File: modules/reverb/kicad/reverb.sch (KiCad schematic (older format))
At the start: 67 parts, among them P1 CONN_01X02, P2 CONN_01X03, P3 CONN_01X02, P4 CONN_01X03, P5 CONN_01X03, P6 CONN_01X02, P7 CONN_01X02, P8 CONN_01X02, P9 CONN_01X02, Q1 2N3906, Q2 2N3906, U1 TL074, U2 TL074, U3 LM386, U4 LM13700

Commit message: Reverb PCB: footprint assignments
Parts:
- added C2, C3: 470u, Capacitors_ThroughHole:CP_Radial_D8.0mm_P3.50mm, symbol CP
- C1: footprint (none) -> Capacitors_ThroughHole:C_Disc_D4.7mm_W2.5mm_P5.00mm
- C10: renamed from C8; footprint (none) -> Capacitors_ThroughHole:C_Disc_D4.7mm_W2.5mm_P5.00mm
- C11: renamed from C9; footprint (none) -> Capacitors_ThroughHole:C_Disc_D4.7mm_W2.5mm_P5.00mm
- C12: renamed from C10; footprint (none) -> Capacitors_ThroughHole:CP_Radial_D4.0mm_P1.50mm
- C13: renamed from C11; footprint (none) -> Capacitors_ThroughHole:C_Disc_D4.7mm_W2.5mm_P5.00mm
- C14: renamed from C12; footprint (none) -> Capacitors_ThroughHole:CP_Radial_D10.0mm_P3.80mm
- C15: renamed from C13; footprint (none) -> Capacitors_ThroughHole:C_Disc_D4.7mm_W2.5mm_P5.00mm
- C16: renamed from C14; footprint (none) -> Capacitors_ThroughHole:C_Disc_D4.7mm_W2.5mm_P5.00mm
- C17: renamed from C15; footprint (none) -> Capacitors_ThroughHole:C_Disc_D4.7mm_W2.5mm_P5.00mm
- C18: renamed from C16; footprint (none) -> Capacitors_ThroughHole:C_Disc_D4.7mm_W2.5mm_P5.00mm
- C4: renamed from C2; footprint (none) -> Capacitors_ThroughHole:CP_Radial_D4.0mm_P1.50mm
- C5: renamed from C3; footprint (none) -> Capacitors_ThroughHole:CP_Radial_D4.0mm_P1.50mm
- C6: renamed from C4; footprint (none) -> Capacitors_ThroughHole:CP_Radial_D4.0mm_P1.50mm
- C7: renamed from C5; footprint (none) -> Capacitors_ThroughHole:CP_Radial_D4.0mm_P1.50mm
- C8: renamed from C6; footprint (none) -> Capacitors_ThroughHole:CP_Radial_D4.0mm_P1.50mm
- C9: renamed from C7; footprint (none) -> Capacitors_ThroughHole:CP_Radial_D4.0mm_P1.50mm
- D1, D2: footprint (none) -> Diodes_ThroughHole:D_DO-35_SOD27_P7.62mm_Horizontal
- P1, P3, P6, P7, P8, P9: footprint (none) -> Connectors_Molex:Molex_KK-6410-02_02x2.54mm_Straight
- P2, P4, P5: footprint (none) -> Connectors_Molex:Molex_KK-6410-03_03x2.54mm_Straight
- Q1, Q2: footprint (none) -> TO_SOT_Packages_THT:TO-92_Inline_Narrow_Oval
- R1, R10, R11, R12, R13, R14, R15, R16, R17, R18, R19, R2, R20, R21, R22, R23, R24, R25, R26, R27, R28, R29, R3, R30, R31, R32, R33, R34, R4, R5, R6, R7, R8, R9: footprint (none) -> Resistors_ThroughHole:R_Axial_DIN0207_L6.3mm_D2.5mm_P7.62mm_Horizontal
- U1: renamed from U2; footprint (none) -> Housings_DIP:DIP-14_W7.62mm_LongPads
- U2: renamed from U1; footprint (none) -> Housings_DIP:DIP-14_W7.62mm_LongPads
- U3: footprint (none) -> Housings_DIP:DIP-8_W7.62mm_LongPads
- U4: footprint (none) -> Housings_DIP:DIP-16_W7.62mm_LongPads
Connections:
- net GND: now also C2.2, C3.1
- net VCC: now also C2.1
- net VEE: now also C3.2
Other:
- moved on the sheet: C4, C5, C6, C7, C8, C9

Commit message: Lay out reverb PCB
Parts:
- C18: value 100n -> 100p
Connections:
- net DRY-SIGNAL: now also U2.14; no longer U2.1
- net GND: now also P1.2 (P2), U1.12 (+), U1.3 (+), U2.10 (+), U2.12 (+), U2.5 (+); no longer P1.1 (P1), U1.10 (+), U1.3 (+), U2.10 (+), U2.12 (+), U2.3 (+)
- net VCC: now also P4.1 (P1); no longer P4.3 (P3)
- net WET-SIGNAL: now also U2.1; no longer U2.7
- net at R10.2, R7.1: now also U2.13 (-); no longer U2.2 (-)
- net at P8.2 (P2), R27.1: now also U2.3 (+); no longer U2.5 (+)
- net at C18.2, R30.1, R31.2: now also U2.2 (-); no longer U2.6 (-)
- net at R32.2, R34.1: now also U2.7; no longer U2.8
- net at R28.2, R29.2, R32.1: now also U2.6 (-); no longer U2.9 (-)
- net at R3.1, R4.1, R8.2: now also U1.13 (-); no longer U1.2 (-)
- net at D1.1 (K), Q1.1 (E), R11.1: now also U1.9 (-); no longer U1.6 (-)
- net at D1.2 (A), Q1.2 (B): now also U1.8; no longer U1.7
- net at R5.1, R6.1, R9.2: now also U1.2 (-); no longer U1.9 (-)
- net at D2.1 (K), Q2.1 (E), R12.1: now also U1.6 (-); no longer U1.13 (-)
- net at D2.2 (A), Q2.2 (B): now also U1.7; no longer U1.14
- net at R3.2: now also P1.1 (P1); no longer P1.2 (P2)
- net at R2.1: now also P4.3 (P3); no longer P4.1 (P1)
- new net: U2.8, U2.9 (-)
- new net: R8.1, U1.10 (+), U1.14
- new net: R9.1, U1.1, U1.5 (+)
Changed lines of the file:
@@
 $Comp
 L TL074 U2
-U 1 1 592C672D
+U 4 1 592C672D
 P 3050 1550
 F 0 "U2" H 3050 1750 50  0000 L CNN
@@
 F 2 "Housings_DIP:DIP-14_W7.62mm_LongPads" H 3000 1650 50  0001 C CNN
 F 3 "" H 3100 1750 50  0000 C CNN
-	1    3050 1550
+	4    3050 1550
 	1    0    0    -1
 $EndComp
 $Comp
 L TL074 U2
-U 2 1 592C67C2
+U 1 1 592C67C2
 P 8200 1450
 F 0 "U2" H 8200 1650 50  0000 L CNN
@@
 F 2 "Housings_DIP:DIP-14_W7.62mm_LongPads" H 8150 1550 50  0001 C CNN
 F 3 "" H 8250 1650 50  0000 C CNN
-	2    8200 1450
+	1    8200 1450
 	1    0    0    -1
 $EndComp
 $Comp
 L TL074 U2
-U 4 1 592C6805
+U 3 1 592C6805
 P 5350 6550
 F 0 "U2" H 5350 6750 50  0000 L CNN
@@
 F 2 "Housings_DIP:DIP-14_W7.62mm_LongPads" H 5300 6650 50  0001 C CNN
 F 3 "" H 5400 6750 50  0000 C CNN
-	4    5350 6550
+	3    5350 6550
 	1    0    0    -1
 $EndComp
 $Comp
 L TL074 U2
-U 3 1 592C6876
+U 2 1 592C6876
 P 8500 3800
 F 0 "U2" H 8500 4000 50  0000 L CNN
@@
 F 2 "Housings_DIP:DIP-14_W7.62mm_LongPads" H 8450 3900 50  0001 C CNN
 F 3 "" H 8550 4000 50  0000 C CNN
-	3    8500 3800
+	2    8500 3800
 	1    0    0    -1
 $EndComp
 $Comp
 L TL074 U1
-U 1 1 592C6A7D
+U 4 1 592C6A7D
 P 2900 3050
 F 0 "U1" H 2900 3250 50  0000 L CNN
@@
 F 2 "Housings_DIP:DIP-14_W7.62mm_LongPads" H 2850 3150 50  0001 C CNN
 F 3 "" H 2950 3250 50  0000 C CNN
-	1    2900 3050
+	4    2900 3050
 	1    0    0    -1
 $EndComp
 $Comp
 L TL074 U1
-U 2 1 592C6AB8
+U 3 1 592C6AB8
 P 3700 3150
 F 0 "U1" H 3700 3350 50  0000 L CNN
@@
 F 2 "Housings_DIP:DIP-14_W7.62mm_LongPads" H 3650 3250 50  0001 C CNN
 F 3 "" H 3750 3350 50  0000 C CNN
-	2    3700 3150
+	3    3700 3150
 	1    0    0    -1
 $EndComp
 $Comp
 L TL074 U1
-U 3 1 592C6B1F
+U 1 1 592C6B1F
 P 2900 4600
 F 0 "U1" H 2900 4800 50  0000 L CNN
@@
 F 2 "Housings_DIP:DIP-14_W7.62mm_LongPads" H 2850 4700 50  0001 C CNN
 F 3 "" H 2950 4800 50  0000 C CNN
-	3    2900 4600
+	1    2900 4600
 	1    0    0    -1
 $EndComp
 $Comp
 L TL074 U1
-U 4 1 592C6B80
+U 2 1 592C6B80
 P 3700 4700
 F 0 "U1" H 3700 4900 50  0000 L CNN
@@
 F 2 "Housings_DIP:DIP-14_W7.62mm_LongPads" H 3650 4800 50  0001 C CNN
 F 3 "" H 3750 4900 50  0000 C CNN
-	4    3700 4700
+	2    3700 4700
 	1    0    0    -1
 $EndComp
@@
 P 8200 2050
 F 0 "C18" H 8225 2150 50  0000 L CNN
-F 1 "100n" H 8250 2200 50  0000 L CNN
+F 1 "100p" H 8250 2200 50  0000 L CNN
 F 2 "Capacitors_ThroughHole:C_Disc_D4.7mm_W2.5mm_P5.00mm" H 8238 1900 50  0001 C CNN
 F 3 "" H 8200 2050 50  0000 C CNN
@@
 F 3 "" H 1650 3000 50  0000 C CNN
 	1    1650 3000
-	-1   0    0    1
+	-1   0    0    -1
 $EndComp
 $Comp
@@
 F 3 "" H 1650 5100 50  0000 C CNN
 	1    1650 5100
-	-1   0    0    1
+	-1   0    0    -1
 $EndComp
 $Comp
@@
 	2300 3150 2600 3150
 Wire Wire Line
-	1850 2950 1950 2950
-Wire Wire Line
-	1850 3050 1900 3050
-Wire Wire Line
 	1900 3050 1900 3100
 Wire Wire Line
@@
 	1900 4600 1900 4650
 Wire Wire Line
-	1850 5000 1900 5000
-Wire Wire Line
-	1900 5000 1900 4950
-Wire Wire Line
-	1850 5200 1900 5200
-Wire Wire Line
-	1900 5200 1900 5250
-Wire Wire Line
 	1900 5600 1900 5550
-Wire Wire Line
-	1850 5100 1950 5100
 Wire Wire Line
 	2300 5100 2250 5100
@@
 	2350 7100 2350 7150
 Connection ~ 2350 7150
+Wire Wire Line
+	1850 5000 1900 5000
+Wire Wire Line
+	1900 5000 1900 4950
+Wire Wire Line
+	1850 5100 1950 5100
+Wire Wire Line
+	1850 5200 1900 5200
+Wire Wire Line
+	1900 5200 1900 5250
+Wire Wire Line
+	1850 2950 1950 2950
+Wire Wire Line
+	1850 3050 1900 3050
 $EndSCHEMATC

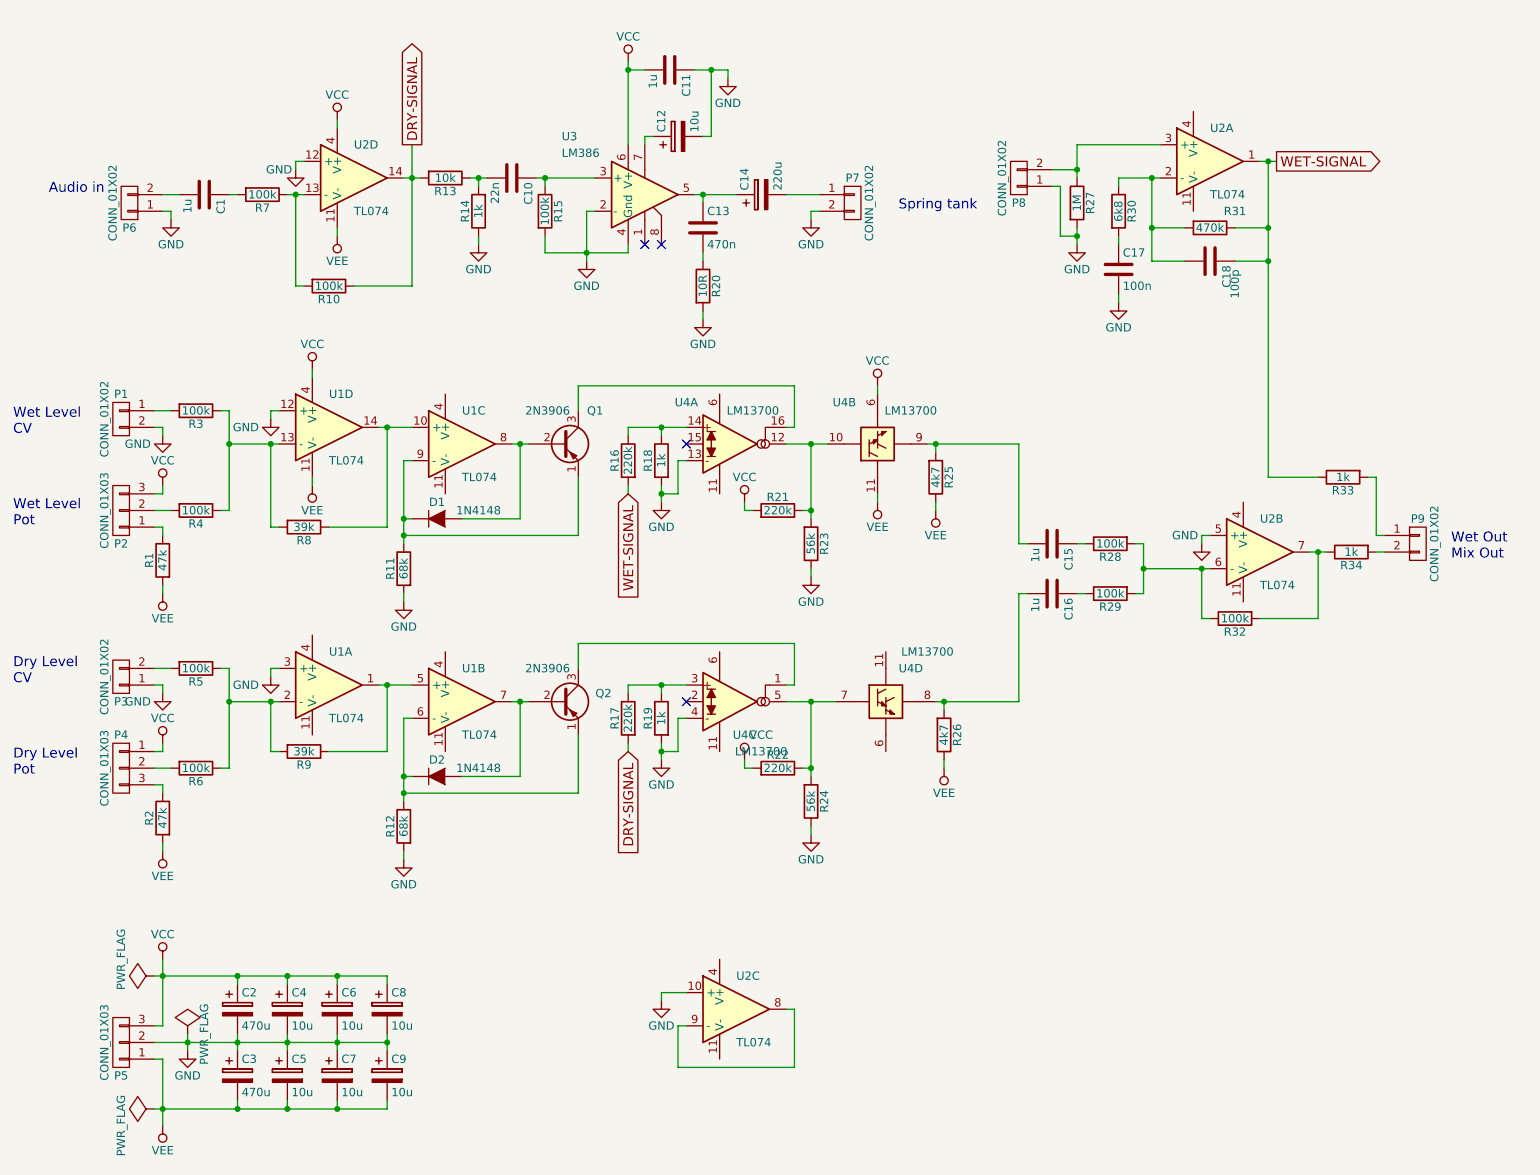
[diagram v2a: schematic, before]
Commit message: Correct some component values on reverb schematic/pcb
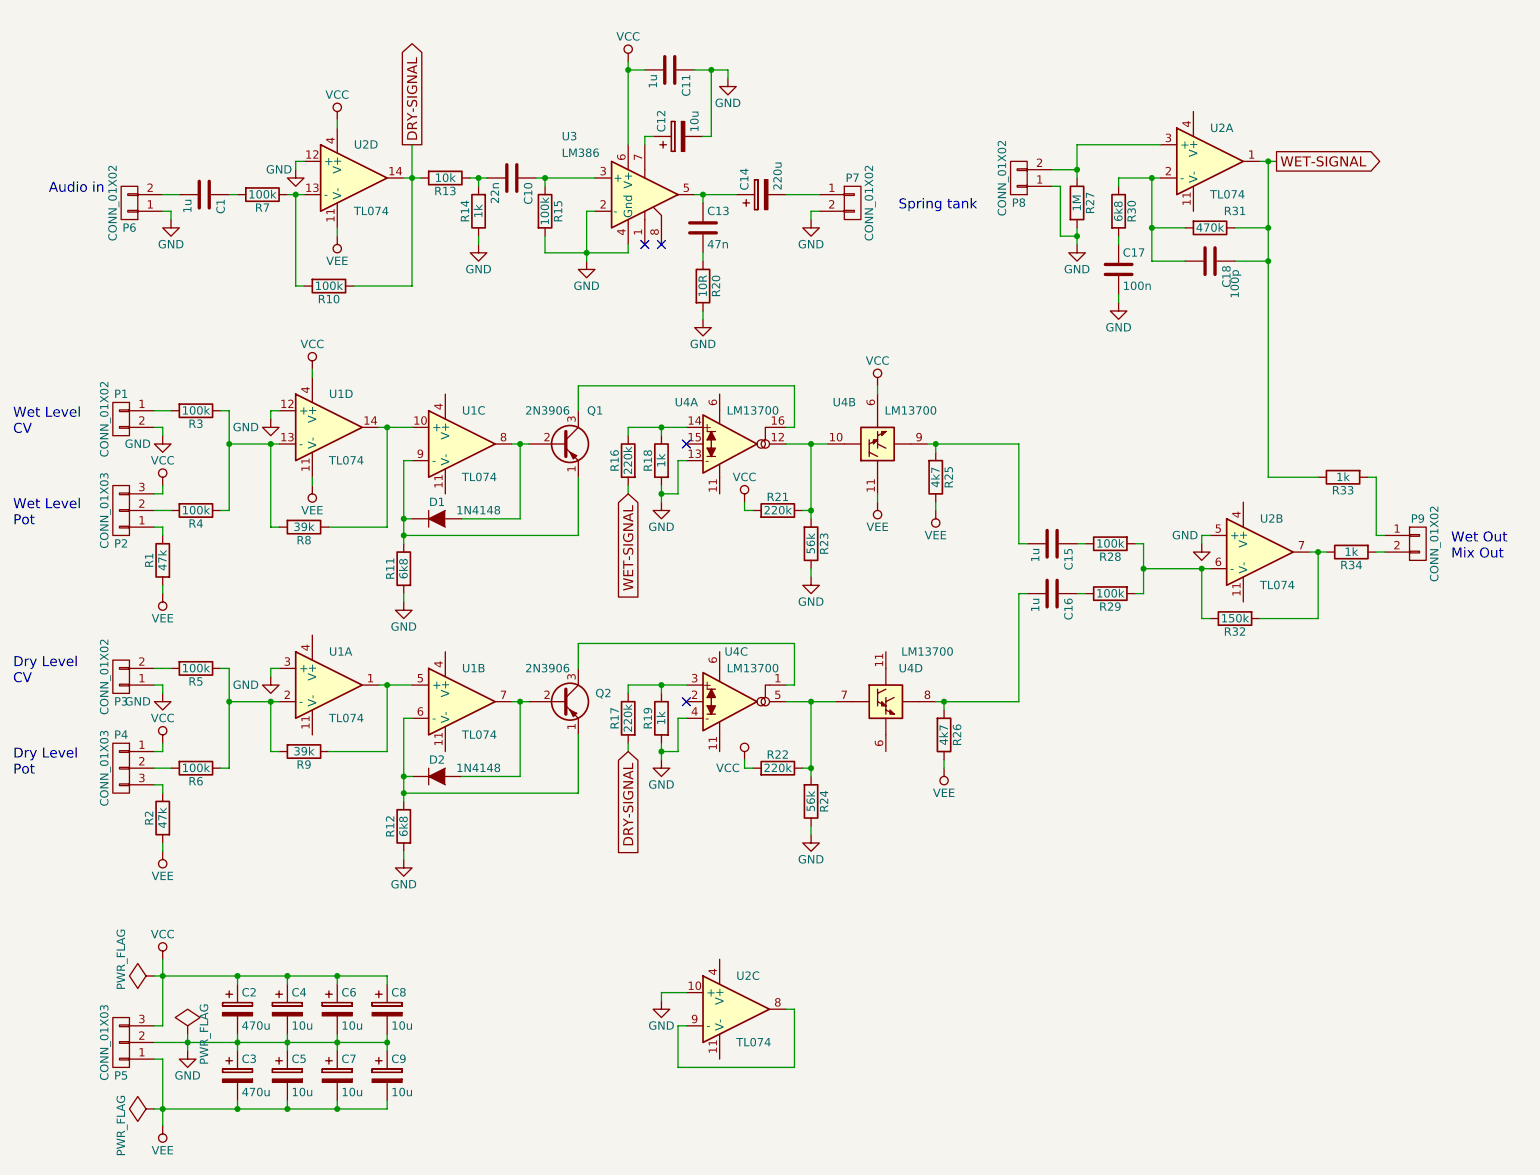
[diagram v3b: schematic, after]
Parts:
- C13: value 470n -> 47n
- R11, R12: value 68k -> 6k8
- R32: value 100k -> 150k
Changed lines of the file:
@@
 U 3 1 592C6E6C
 P 5250 4700
-F 0 "U4" H 5400 4900 50  0000 C CNN
-F 1 "LM13700" H 5500 5000 50  0000 C CNN
+F 0 "U4" H 5350 4400 50  0000 C CNN
+F 1 "LM13700" H 5450 4500 50  0000 C CNN
 F 2 "Housings_DIP:DIP-16_W7.62mm_LongPads" H 5150 4725 50  0001 C CNN
 F 3 "" H 5150 4725 50  0000 C CNN
@@
 P 5150 1850
 F 0 "C13" H 5175 1950 50  0000 L CNN
-F 1 "470n" H 5175 1750 50  0000 L CNN
+F 1 "47n" H 5175 1750 50  0000 L CNN
 F 2 "Capacitors_ThroughHole:C_Disc_D4.7mm_W2.5mm_P5.00mm" H 5188 1700 50  0001 C CNN
 F 3 "" H 5150 1850 50  0000 C CNN
@@
 P 3350 3900
 F 0 "R11" V 3430 3900 50  0000 C CNN
-F 1 "68k" V 3350 3900 50  0000 C CNN
+F 1 "6k8" V 3350 3900 50  0000 C CNN
 F 2 "Resistors_ThroughHole:R_Axial_DIN0207_L6.3mm_D2.5mm_P7.62mm_Horizontal" V 3280 3900 50  0001 C CNN
 F 3 "" H 3350 3900 50  0000 C CNN
@@
 P 3350 5450
 F 0 "R12" V 3430 5450 50  0000 C CNN
-F 1 "68k" V 3350 5450 50  0000 C CNN
+F 1 "6k8" V 3350 5450 50  0000 C CNN
 F 2 "Resistors_ThroughHole:R_Axial_DIN0207_L6.3mm_D2.5mm_P7.62mm_Horizontal" V 3280 5450 50  0001 C CNN
 F 3 "" H 3350 5450 50  0000 C CNN
@@
 P 5400 5050
 F 0 "#PWR033" H 5400 4900 50  0001 C CNN
-F 1 "VCC" H 5500 5200 50  0000 C CNN
+F 1 "VCC" H 5300 5000 50  0000 C CNN
 F 2 "" H 5400 5050 50  0000 C CNN
 F 3 "" H 5400 5050 50  0000 C CNN
@@
 P 8350 4200
 F 0 "R32" V 8430 4200 50  0000 C CNN
-F 1 "100k" V 8350 4200 50  0000 C CNN
+F 1 "150k" V 8350 4200 50  0000 C CNN
 F 2 "Resistors_ThroughHole:R_Axial_DIN0207_L6.3mm_D2.5mm_P7.62mm_Horizontal" V 8280 4200 50  0001 C CNN
 F 3 "" H 8350 4200 50  0000 C CNN

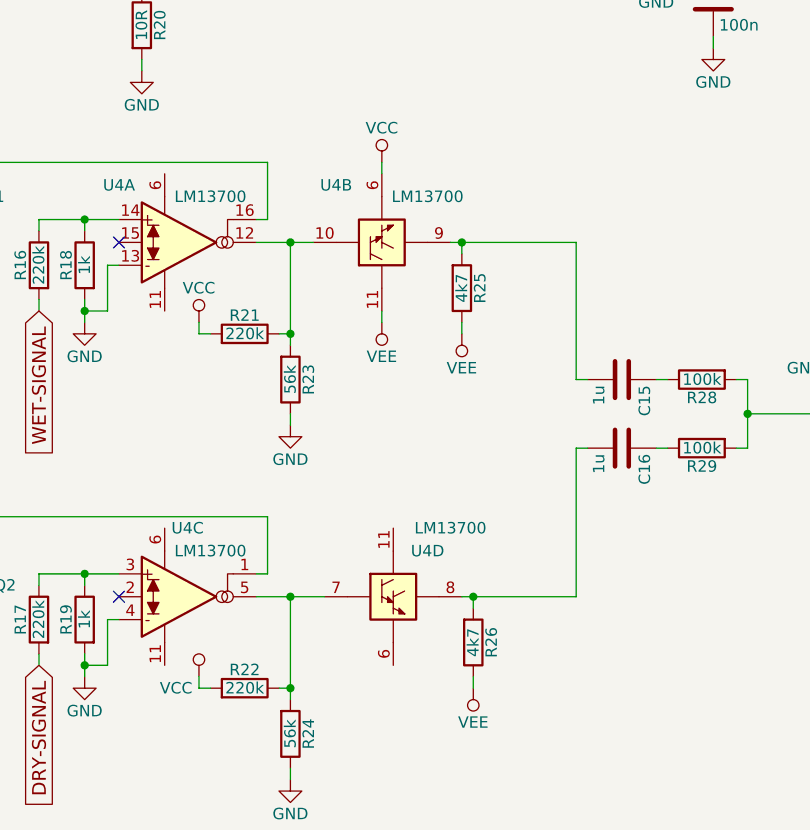
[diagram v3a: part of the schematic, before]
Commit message: Reverb: Fix LM13700 power connections inverted
The power pins on the LM13700 OTA were the wrong way around. This causes
the LM13700 to, well, break. it'll heat up a bit and of course not
function.
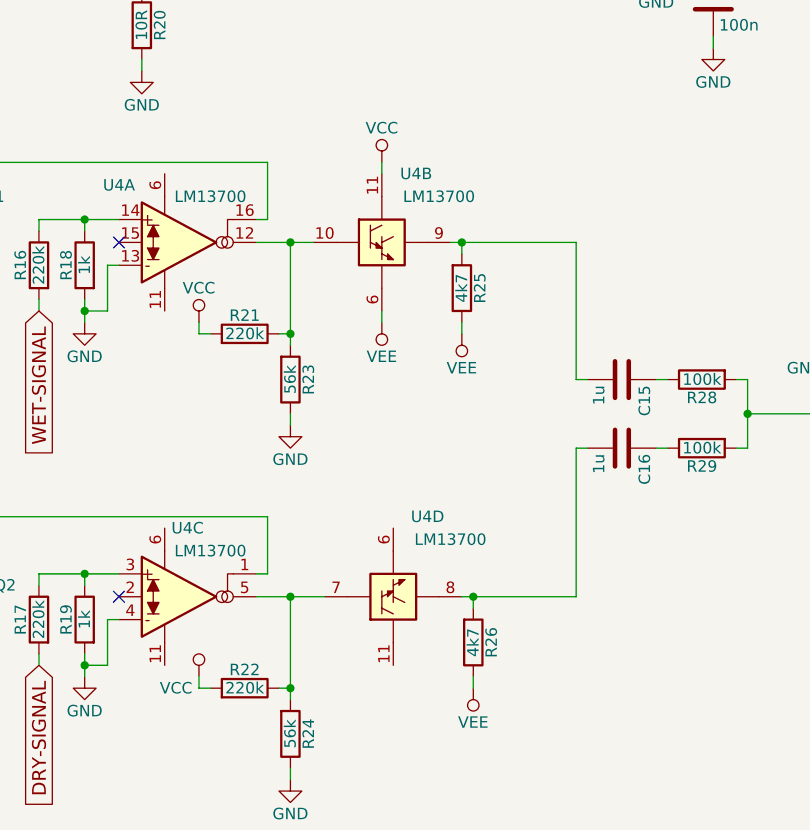
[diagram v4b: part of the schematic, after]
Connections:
- net VCC: now also U4.11 (V+); no longer U4.6 (V-)
- net VEE: now also U4.6 (V-); no longer U4.11 (V+)
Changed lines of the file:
@@
 U 2 1 592C6EC1
 P 6200 3150
-F 0 "U4" H 6000 2900 50  0000 C CNN
-F 1 "LM13700" H 6400 2950 50  0000 C CNN
+F 0 "U4" H 6350 3450 50  0000 C CNN
+F 1 "LM13700" H 6450 3350 50  0000 C CNN
 F 2 "Housings_DIP:DIP-16_W7.62mm_LongPads" H 6100 3175 50  0001 C CNN
 F 3 "" H 6100 3175 50  0000 C CNN
 	2    6200 3150
-	1    0    0    1
+	1    0    0    -1
 $EndComp
 $Comp
@@
 U 4 1 592C6F04
 P 6250 4700
-F 0 "U4" H 6400 4900 50  0000 C CNN
-F 1 "LM13700" H 6500 5000 50  0000 C CNN
+F 0 "U4" H 6400 4350 50  0000 C CNN
+F 1 "LM13700" H 6500 4450 50  0000 C CNN
 F 2 "Housings_DIP:DIP-16_W7.62mm_LongPads" H 6150 4725 50  0001 C CNN
 F 3 "" H 6150 4725 50  0000 C CNN
 	4    6250 4700
-	1    0    0    -1
+	1    0    0    1
 $EndComp
 $Comp
@@
 Connection ~ 5800 3150
 Wire Wire Line
-	6200 3500 6200 3450
-Wire Wire Line
-	6200 2850 6200 2800
-Wire Wire Line
 	5400 3500 5400 3550
 Wire Wire Line
@@
 Wire Wire Line
 	1850 3050 1900 3050
+Wire Wire Line
+	6200 2850 6200 2800
+Wire Wire Line
+	6200 3450 6200 3500
 $EndSCHEMATC
